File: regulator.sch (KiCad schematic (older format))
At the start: 33 parts, among them Q201 IRF7343PBF, U201 358, U202 358

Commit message: Changed a bit, and did a full re-route
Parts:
- removed C203: CP, Capacitors_ThroughHole:C_Radial_D10_L16_P5, symbol CP
- removed D206: D, Diodes_ThroughHole:Diode_DO-41_SOD81_Vertical_KathodeUp, symbol D
- removed L202: L, Inductors_NEOSID:Neosid_Inductor_Sd14, symbol L
- removed R218: R, Resistors_SMD:R_0805, symbol R
- added D206, D207: D_Schottky, lib:Diode_DO-201AD_Vertical, symbol D_Schottky
- added TP201, TP202: TEST, Measurement_Points:Measurement_Point_Round-SMD-Pad_Big, symbol TEST
- C201, C202: value CP -> 100uF; farnell (none) -> 1281843
- D201, D205: footprint Diodes_ThroughHole:Diode_DO-41_SOD81_Vertical_KathodeUp -> Diodes_SMD:SOD-323_HandSoldering; farnell (none) -> 2441312
- D202, D203, D204: footprint Diodes_ThroughHole:Diode_DO-201AD_Horizontal_RM15 -> lib:Diode_DO-201AD_Vertical
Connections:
- net labels added: in_rect+, in_rect-
- wire segments 70 -> 67
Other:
- note added: "if we are motoring backwards\nwe will also generate power\nThe mcu should detect higher voltage, \nand stop charging"
- note removed: "if we are motoring backwards\nwe will generate backwards power"
- note removed: "load for when we are going backwards, \nto make sure that the generator has something to do\nand doesn't start generating 60V\nalso, if we are going backwards, it is on engine, \nso we don't care about power because we have\na 60A alternator :|"
- note removed: "probably not necessary..."
- note removed: "we don't want our motor driving our generator :|\n"
- moved on the sheet: C201, C202, D202, R210, R211, R212, R213, R214, U202A, U202B

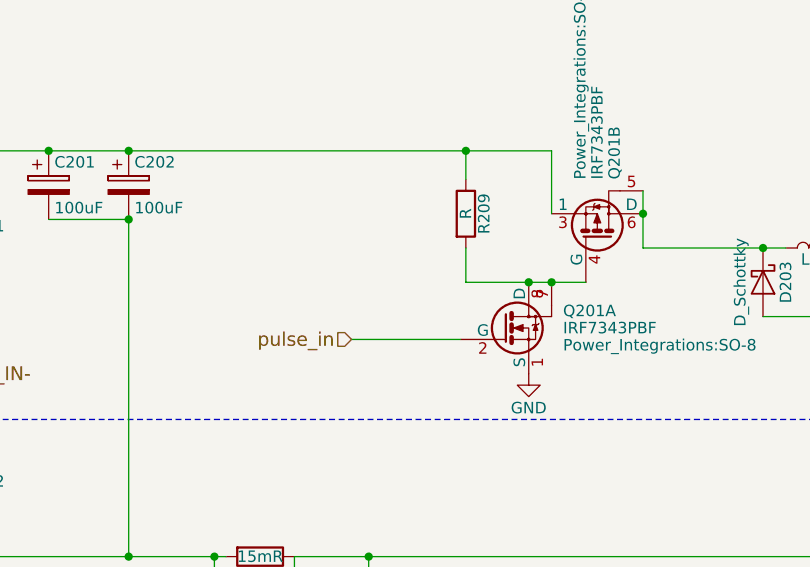
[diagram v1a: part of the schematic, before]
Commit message: Routed for 5x5 pcb
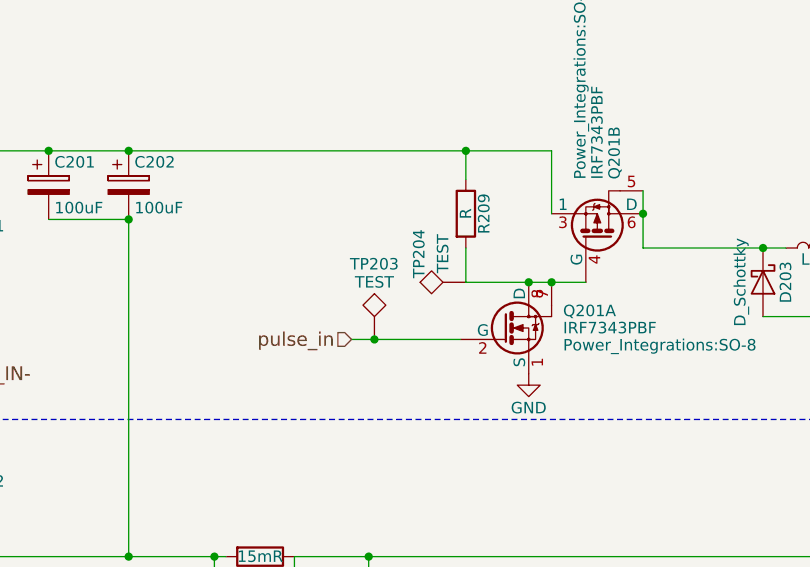
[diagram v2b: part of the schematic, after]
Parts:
- added TP203, TP204: TEST, Measurement_Points:Measurement_Point_Round-SMD-Pad_Big, symbol TEST
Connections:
- net pulse_in: now also TP203.1
- net at Q201.4 (G), Q201.7, Q201.8 (D)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: now also TP204.1
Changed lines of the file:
@@
 EESchema Schematic File Version 2
+LIBS:linearPower
 LIBS:power
 LIBS:device
@@
 $EndComp
 $Comp
-L GND #PWR013
+L GND #PWR206
 U 1 1 58502E64
 P 5225 2650
-F 0 "#PWR013" H 5225 2400 50  0001 C CNN
+F 0 "#PWR206" H 5225 2400 50  0001 C CNN
 F 1 "GND" H 5225 2500 50  0000 C CNN
 F 2 "" H 5225 2650 50  0000 C CNN
@@
 $EndComp
 $Comp
-L GND #PWR014
+L GND #PWR207
 U 1 1 58504D82
 P 6725 2400
-F 0 "#PWR014" H 6725 2150 50  0001 C CNN
+F 0 "#PWR207" H 6725 2150 50  0001 C CNN
 F 1 "GND" H 6725 2250 50  0000 C CNN
 F 2 "" H 6725 2400 50  0000 C CNN
@@
 BATTERY-
 $Comp
-L GND #PWR015
+L GND #PWR209
 U 1 1 585070B4
 P 7100 3500
-F 0 "#PWR015" H 7100 3250 50  0001 C CNN
+F 0 "#PWR209" H 7100 3250 50  0001 C CNN
 F 1 "GND" H 7100 3350 50  0000 C CNN
 F 2 "" H 7100 3500 50  0000 C CNN
@@
 $EndComp
 $Comp
-L +24V #PWR016
+L +24V #PWR208
 U 1 1 585084CF
 P 6900 4025
-F 0 "#PWR016" H 6900 3875 50  0001 C CNN
+F 0 "#PWR208" H 6900 3875 50  0001 C CNN
 F 1 "+24V" H 6900 4165 50  0000 C CNN
 F 2 "" H 6900 4025 50  0000 C CNN
@@
 $EndComp
 $Comp
-L +24V #PWR017
+L +24V #PWR211
 U 1 1 58508565
 P 8525 2100
-F 0 "#PWR017" H 8525 1950 50  0001 C CNN
+F 0 "#PWR211" H 8525 1950 50  0001 C CNN
 F 1 "+24V" H 8525 2240 50  0000 C CNN
 F 2 "" H 8525 2100 50  0000 C CNN
@@
 $EndComp
 $Comp
-L GND #PWR018
+L GND #PWR202
 U 1 1 58509A2F
 P 2650 7050
-F 0 "#PWR018" H 2650 6800 50  0001 C CNN
+F 0 "#PWR202" H 2650 6800 50  0001 C CNN
 F 1 "GND" H 2650 6900 50  0000 C CNN
 F 2 "" H 2650 7050 50  0000 C CNN
@@
 Ubat
 $Comp
-L GNDA #PWR019
+L GNDA #PWR210
 U 1 1 5850AF60
 P 8125 5575
-F 0 "#PWR019" H 8125 5325 50  0001 C CNN
+F 0 "#PWR210" H 8125 5325 50  0001 C CNN
 F 1 "GNDA" H 8125 5425 50  0000 C CNN
 F 2 "" H 8125 5575 50  0000 C CNN
@@
 $EndComp
 $Comp
-L GND #PWR020
+L GND #PWR205
 U 1 1 58510A94
 P 4525 3500
-F 0 "#PWR020" H 4525 3250 50  0001 C CNN
+F 0 "#PWR205" H 4525 3250 50  0001 C CNN
 F 1 "GND" H 4525 3350 50  0000 C CNN
 F 2 "" H 4525 3500 50  0000 C CNN
@@
 gain of 40, and shunt of 0.015. \nSo 1A gives 1*0.015*40=0.6v
 $Comp
-L GNDA #PWR021
+L GNDA #PWR204
 U 1 1 58510AA8
 P 4500 5575
-F 0 "#PWR021" H 4500 5325 50  0001 C CNN
+F 0 "#PWR204" H 4500 5325 50  0001 C CNN
 F 1 "GNDA" H 4500 5425 50  0000 C CNN
 F 2 "" H 4500 5575 50  0000 C CNN
@@
 gain of 40, and shunt of 0.015. \nSo 1A gives 1*0.015*40=0.6v
 $Comp
-L +24V #PWR022
+L +24V #PWR203
 U 1 1 585143D9
 P 4000 4025
-F 0 "#PWR022" H 4000 3875 50  0001 C CNN
+F 0 "#PWR203" H 4000 3875 50  0001 C CNN
 F 1 "+24V" H 4000 4165 50  0000 C CNN
 F 2 "" H 4000 4025 50  0000 C CNN
@@
 $EndComp
 $Comp
-L GND #PWR023
+L GND #PWR212
 U 1 1 5852D1BD
 P 10025 5825
-F 0 "#PWR023" H 10025 5575 50  0001 C CNN
+F 0 "#PWR212" H 10025 5575 50  0001 C CNN
 F 1 "GND" H 10025 5675 50  0000 C CNN
 F 2 "" H 10025 5825 50  0000 C CNN
@@
 maybe: \nhttp://nl.farnell.com/coilcraft/pcv-0-154-05l/inductor-power-150uh-5-2a-10/dp/2457654
 $Comp
-L GNDA #PWR024
+L GNDA #PWR201
 U 1 1 5857DF75
 P 1950 7200
-F 0 "#PWR024" H 1950 6950 50  0001 C CNN
+F 0 "#PWR201" H 1950 6950 50  0001 C CNN
 F 1 "GNDA" H 1950 7050 50  0000 C CNN
 F 2 "" H 1950 7200 50  0000 C CNN
@@
 $EndComp
 $Comp
-L GNDA #PWR025
+L GNDA #PWR213
 U 1 1 5857E3C4
 P 10675 5975
-F 0 "#PWR025" H 10675 5725 50  0001 C CNN
+F 0 "#PWR213" H 10675 5725 50  0001 C CNN
 F 1 "GNDA" H 10675 5825 50  0000 C CNN
 F 2 "" H 10675 5975 50  0000 C CNN
@@
 Connection ~ 7100 3450
 Connection ~ 4525 3450
+$Comp
+L TEST TP203
+U 1 1 587C17AD
+P 4550 2500
+F 0 "TP203" H 4550 2800 50  0000 C BNN
+F 1 "TEST" H 4550 2750 50  0000 C CNN
+F 2 "Measurement_Points:Measurement_Point_Round-SMD-Pad_Big" H 4550 2500 50  0001 C CNN
+F 3 "" H 4550 2500 50  0000 C CNN
+	1    4550 2500
+	1    0    0    -1
+$EndComp
+$Comp
+L TEST TP204
+U 1 1 587C1904
+P 4950 2250
+F 0 "TP204" H 5075 2425 50  0000 C BNN
+F 1 "TEST" H 5075 2350 50  0000 C CNN
+F 2 "Measurement_Points:Measurement_Point_Round-SMD-Pad_Big" H 4950 2250 50  0001 C CNN
+F 3 "" H 4950 2250 50  0000 C CNN
+	1    4950 2250
+	0    -1   -1   0
+$EndComp
+Connection ~ 4550 2500
 $EndSCHEMATC

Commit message: Rerouted, and made everything beautifull
 - added screw bolt-holes for the output.
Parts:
- removed D203: D_Schottky, lib:Diode_DO-201AD_Vertical, symbol D_Schottky
- removed Q201: IRF7343PBF, Power_Integrations:SO-8, symbol IRF7343PBF
- added C203, C205, C206, C207: 100nF, Capacitors_SMD:C_0805, symbol C
- added D203: STPS10H100C, TO_SOT_Packages_THT:TO-220_Vertical, symbol D_x2_KCom_AKA
- added Q201: 2n7002, TO_SOT_Packages_SMD:SOT-23, symbol Q_NMOS_GSD
- added Q202: STD35P6LLF6, TO_SOT_Packages_SMD:TO-252-2Lead, symbol Q_PMOS_GDS
- added R218, R219: 10k, Resistors_SMD:R_0805, symbol R
- C201, C202: footprint Capacitors_ThroughHole:C_Radial_D10_L16_P5 -> Capacitors_ThroughHole:CP_Radial_D10.0mm_P2.50mm
- C204: footprint Capacitors_ThroughHole:C_Radial_D8_L21_P3.8 -> Capacitors_ThroughHole:CP_Radial_D8.0mm_P5.00mm
- D201, D205: footprint Diodes_SMD:SOD-323_HandSoldering -> Diodes_SMD:D_SOD-323_HandSoldering
- L201: footprint Inductors_NEOSID:Neosid_Inductor_Sd14 -> lib:toroid
- R209: value R -> 1k
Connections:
- net GND: now also C201.2, D203.1 (A), D203.3 (A), Q201.2 (S)
- net GNDA: now also C203.2, C205.2, C206.2, C207.2
- net Iin: now also C205.1, R218.2; no longer R204.2, U201.1
- net Iout: now also C206.1, R219.2; no longer R210.2, U202.1
- net Ubat: now also C207.1
- net Uin: now also C203.1
- net in_rect+: now also Q202.3 (S)
- net in_rect-: no longer C201.2
- net pulse_in: now also Q201.1 (G)
- net at R209.2, TP204.1: now also Q201.3 (D), Q202.1 (G)
- net switchpool: now reaches L201.1
- net switchpool: now also D203.2 (K), Q202.2 (D)
- new net: R210.2, R219.1, U202.1
- new net: R204.2, R218.1, U201.1
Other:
- moved on the sheet: C201, C204, L201, TP203

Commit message: Added small display.
And made everything look even nicer
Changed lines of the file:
@@
 LIBS:valves
 LIBS:stm32
-LIBS:main-cache
 LIBS:mppt-cache
 EELAYER 25 0
@@
 $Descr A4 11693 8268
 encoding utf-8
-Sheet 2 3
+Sheet 2 4
 Title ""
 Date ""
@@
 $EndComp
 $Comp
-L GND #PWR014
+L GND #PWR012
 U 1 1 58502E64
 P 5225 2650
-F 0 "#PWR014" H 5225 2400 50  0001 C CNN
+F 0 "#PWR012" H 5225 2400 50  0001 C CNN
 F 1 "GND" H 5225 2500 50  0000 C CNN
 F 2 "" H 5225 2650 50  0000 C CNN
@@
 BATTERY-
 $Comp
-L GND #PWR015
+L GND #PWR013
 U 1 1 585070B4
 P 7100 3500
-F 0 "#PWR015" H 7100 3250 50  0001 C CNN
+F 0 "#PWR013" H 7100 3250 50  0001 C CNN
 F 1 "GND" H 7100 3350 50  0000 C CNN
 F 2 "" H 7100 3500 50  0000 C CNN
@@
 $EndComp
 $Comp
-L +24V #PWR016
+L +24V #PWR014
 U 1 1 585084CF
 P 6900 4025
-F 0 "#PWR016" H 6900 3875 50  0001 C CNN
+F 0 "#PWR014" H 6900 3875 50  0001 C CNN
 F 1 "+24V" H 6900 4165 50  0000 C CNN
 F 2 "" H 6900 4025 50  0000 C CNN
@@
 $EndComp
 $Comp
-L +24V #PWR017
+L +24V #PWR015
 U 1 1 58508565
 P 8825 1950
-F 0 "#PWR017" H 8825 1800 50  0001 C CNN
+F 0 "#PWR015" H 8825 1800 50  0001 C CNN
 F 1 "+24V" H 8825 2090 50  0000 C CNN
 F 2 "" H 8825 1950 50  0000 C CNN
@@
 $EndComp
 $Comp
-L GND #PWR018
+L GND #PWR016
 U 1 1 58509A2F
 P 2650 7050
-F 0 "#PWR018" H 2650 6800 50  0001 C CNN
+F 0 "#PWR016" H 2650 6800 50  0001 C CNN
 F 1 "GND" H 2650 6900 50  0000 C CNN
 F 2 "" H 2650 7050 50  0000 C CNN
@@
 Ubat
 $Comp
-L GNDA #PWR019
+L GNDA #PWR017
 U 1 1 5850AF60
 P 8125 5575
-F 0 "#PWR019" H 8125 5325 50  0001 C CNN
+F 0 "#PWR017" H 8125 5325 50  0001 C CNN
 F 1 "GNDA" H 8125 5425 50  0000 C CNN
 F 2 "" H 8125 5575 50  0000 C CNN
@@
 $EndComp
 $Comp
-L GND #PWR020
+L GND #PWR018
 U 1 1 58510A94
 P 4525 3500
-F 0 "#PWR020" H 4525 3250 50  0001 C CNN
+F 0 "#PWR018" H 4525 3250 50  0001 C CNN
 F 1 "GND" H 4525 3350 50  0000 C CNN
 F 2 "" H 4525 3500 50  0000 C CNN
@@
 gain of 40, and shunt of 0.015. \nSo 1A gives 1*0.015*40=0.6v
 $Comp
-L GNDA #PWR021
+L GNDA #PWR019
 U 1 1 58510AA8
 P 4500 5575
-F 0 "#PWR021" H 4500 5325 50  0001 C CNN
+F 0 "#PWR019" H 4500 5325 50  0001 C CNN
 F 1 "GNDA" H 4500 5425 50  0000 C CNN
 F 2 "" H 4500 5575 50  0000 C CNN
@@
 gain of 40, and shunt of 0.015. \nSo 1A gives 1*0.015*40=0.6v
 $Comp
-L +24V #PWR022
+L +24V #PWR020
 U 1 1 585143D9
 P 4000 4025
-F 0 "#PWR022" H 4000 3875 50  0001 C CNN
+F 0 "#PWR020" H 4000 3875 50  0001 C CNN
 F 1 "+24V" H 4000 4165 50  0000 C CNN
 F 2 "" H 4000 4025 50  0000 C CNN
@@
 $EndComp
 $Comp
-L GND #PWR023
+L GND #PWR021
 U 1 1 5852D1BD
 P 10025 5825
-F 0 "#PWR023" H 10025 5575 50  0001 C CNN
+F 0 "#PWR021" H 10025 5575 50  0001 C CNN
 F 1 "GND" H 10025 5675 50  0000 C CNN
 F 2 "" H 10025 5825 50  0000 C CNN
@@
 maybe: \nhttp://nl.farnell.com/coilcraft/pcv-0-154-05l/inductor-power-150uh-5-2a-10/dp/2457654
 $Comp
-L GNDA #PWR024
+L GNDA #PWR022
 U 1 1 5857DF75
 P 1950 7200
-F 0 "#PWR024" H 1950 6950 50  0001 C CNN
+F 0 "#PWR022" H 1950 6950 50  0001 C CNN
 F 1 "GNDA" H 1950 7050 50  0000 C CNN
 F 2 "" H 1950 7200 50  0000 C CNN
@@
 $EndComp
 $Comp
-L GNDA #PWR025
+L GNDA #PWR023
 U 1 1 5857E3C4
 P 10675 5975
-F 0 "#PWR025" H 10675 5725 50  0001 C CNN
+F 0 "#PWR023" H 10675 5725 50  0001 C CNN
 F 1 "GNDA" H 10675 5825 50  0000 C CNN
 F 2 "" H 10675 5975 50  0000 C CNN
@@
 	2200 6750 1950 6750
 Wire Wire Line
-	2500 6750 2650 6750
-Wire Wire Line
-	2650 6750 2900 6750
-Wire Wire Line
-	2900 6750 3075 6750
-Wire Wire Line
-	6950 1950 7250 1950
-Wire Wire Line
-	7250 1950 8825 1950
-Wire Wire Line
-	8825 1950 8900 1950
-Wire Wire Line
-	4950 2250 5225 2250
-Wire Wire Line
-	5225 2250 5525 2250
-Wire Wire Line
-	2075 1675 2825 1675
-Wire Wire Line
-	2825 1675 3475 1675
-Wire Wire Line
-	3475 1675 3900 1675
-Wire Wire Line
-	3900 1675 4950 1675
-Wire Wire Line
-	4950 1675 5325 1675
+	2500 6750 3075 6750
+Wire Wire Line
+	6950 1950 8900 1950
+Wire Wire Line
+	4950 2250 5525 2250
+Wire Wire Line
+	2075 1675 5325 1675
 Connection ~ 3900 1675
 Connection ~ 3475 1675
@@
 	5325 1675 5325 1950
 Wire Wire Line
-	5725 1950 6300 1950
-Wire Wire Line
-	6300 1950 6650 1950
+	5725 1950 6650 1950
 Connection ~ 6300 1950
 Connection ~ 5725 1950
@@
 	7100 3450 7100 3500
 Wire Wire Line
-	4200 3450 4325 3450
-Wire Wire Line
-	4325 3450 4525 3450
-Wire Wire Line
-	4525 3450 7100 3450
-Wire Wire Line
-	7100 3450 7250 3450
-Wire Wire Line
-	7250 3450 7475 3450
-Wire Wire Line
-	4450 2450 4550 2450
-Wire Wire Line
-	4550 2450 4925 2450
+	4200 3450 7475 3450
+Wire Wire Line
+	4450 2450 4925 2450
 Wire Wire Line
 	6900 4025 7575 4025
 Wire Wire Line
-	7675 4425 7875 4425
-Wire Wire Line
-	7875 4425 8275 4425
+	7675 4425 8275 4425
 Wire Wire Line
 	8275 4425 8275 3825
@@
 Connection ~ 9725 5525
 Wire Wire Line
-	1950 6600 1950 6750
-Wire Wire Line
-	1950 6750 1950 6900
+	1950 6600 1950 6900
 Connection ~ 1950 6750
 Connection ~ 3475 1975
 Wire Wire Line
-	7575 6000 7875 6000
-Wire Wire Line
-	7875 6000 8350 6000
+	7575 6000 8350 6000
 Wire Wire Line
 	1375 6075 1950 6075
@@
 	10425 5525 10675 5525
 Wire Wire Line
-	9525 5525 9725 5525
-Wire Wire Line
-	9725 5525 10025 5525
-Wire Wire Line
-	10025 5525 10125 5525
-Wire Wire Line
-	10675 5375 10675 5525
-Wire Wire Line
-	10675 5525 10675 5675
+	9525 5525 10125 5525
+Wire Wire Line
+	10675 5375 10675 5675
 Connection ~ 10675 5525
 Wire Notes Line
 	950  2850 11450 2850
 Wire Wire Line
-	1775 3450 2825 3450
-Wire Wire Line
-	2825 3450 3475 3450
-Wire Wire Line
-	3475 3450 3850 3450
-Wire Wire Line
-	3850 3450 3900 3450
+	1775 3450 3900 3450
 Wire Wire Line
 	3850 4975 3850 4900
@@
 	3850 3450 3850 4600
 Wire Wire Line
-	4050 4425 4300 4425
-Wire Wire Line
-	4300 4425 4650 4425
+	4050 4425 4650 4425
 Wire Wire Line
 	4050 4425 4050 4600
@@
 $EndComp
 $Comp
-L GNDA #PWR026
+L GNDA #PWR024
 U 1 1 588FE91A
 P 7875 6300
-F 0 "#PWR026" H 7875 6050 50  0001 C CNN
+F 0 "#PWR024" H 7875 6050 50  0001 C CNN
 F 1 "GNDA" H 7875 6150 50  0000 C CNN
 F 2 "" H 7875 6300 50  0000 C CNN
@@
 $EndComp
 $Comp
-L GNDA #PWR027
+L GNDA #PWR025
 U 1 1 588FE97E
 P 3950 6300
-F 0 "#PWR027" H 3950 6050 50  0001 C CNN
+F 0 "#PWR025" H 3950 6050 50  0001 C CNN
 F 1 "GNDA" H 3950 6150 50  0000 C CNN
 F 2 "" H 3950 6300 50  0000 C CNN
@@
 $EndComp
 $Comp
-L GNDA #PWR028
+L GNDA #PWR026
 U 1 1 588FF0CF
 P 2900 7050
-F 0 "#PWR028" H 2900 6800 50  0001 C CNN
+F 0 "#PWR026" H 2900 6800 50  0001 C CNN
 F 1 "GNDA" H 2900 6900 50  0000 C CNN
 F 2 "" H 2900 7050 50  0000 C CNN
@@
 $EndComp
 $Comp
-L GNDA #PWR029
+L GNDA #PWR027
 U 1 1 588FF571
 P 9725 5825
-F 0 "#PWR029" H 9725 5575 50  0001 C CNN
+F 0 "#PWR027" H 9725 5575 50  0001 C CNN
 F 1 "GNDA" H 9725 5675 50  0000 C CNN
 F 2 "" H 9725 5825 50  0000 C CNN
@@
 $EndComp
 $Comp
-L GND #PWR030
+L GND #PWR028
 U 1 1 58A648C6
 P 6600 2150
-F 0 "#PWR030" H 6600 1900 50  0001 C CNN
+F 0 "#PWR028" H 6600 1900 50  0001 C CNN
 F 1 "GND" H 6600 2000 50  0000 C CNN
 F 2 "" H 6600 2150 50  0001 C CNN
@@
 $EndComp
 $Comp
-L GND #PWR031
+L GND #PWR029
 U 1 1 58A6495C
 P 6000 2150
-F 0 "#PWR031" H 6000 1900 50  0001 C CNN
+F 0 "#PWR029" H 6000 1900 50  0001 C CNN
 F 1 "GND" H 6000 2000 50  0000 C CNN
 F 2 "" H 6000 2150 50  0001 C CNN
